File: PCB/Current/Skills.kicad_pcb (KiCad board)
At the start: 2 copper layers, 70 x 85 mm, 68 parts, among them J1 BATT, J2 USB_C_Receptacle_USB2.0, J3 SPI, J4 L, J5 R, U1 TPS61088, U2 FS312F, U3 FS8205A, U4 TP4056, U5 F-3188, U6 MAX9744, U7 ME6209

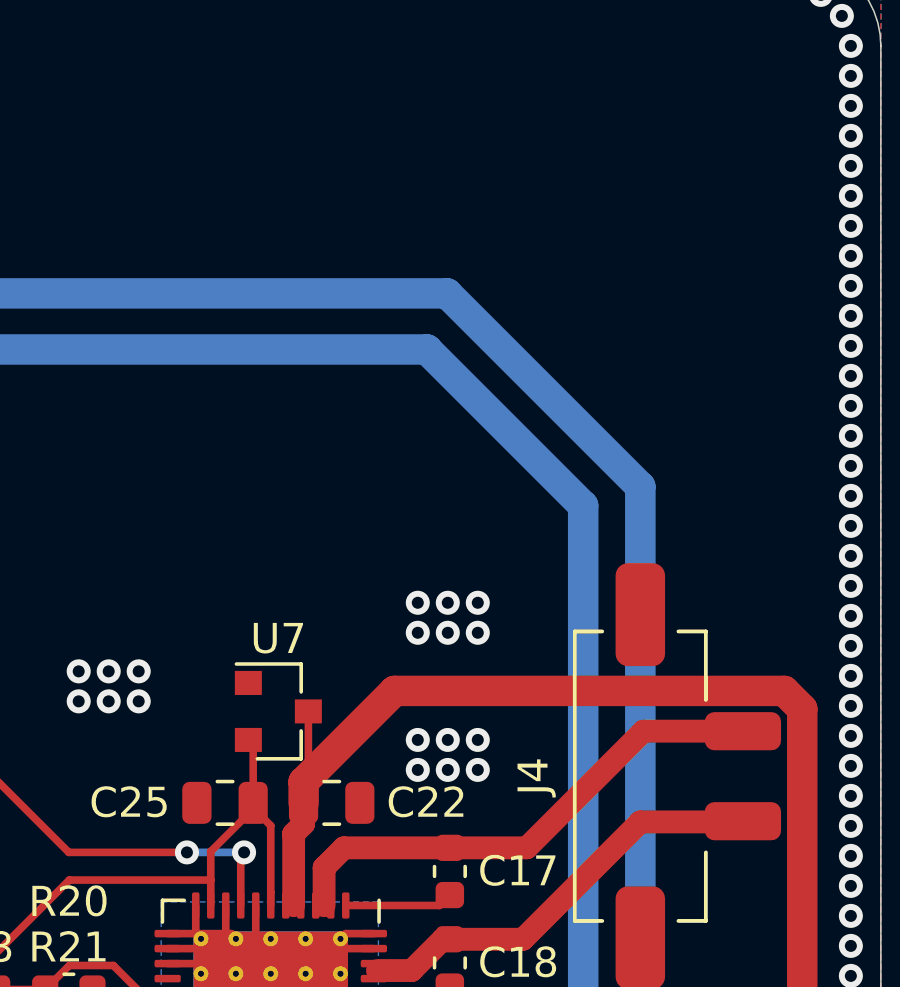
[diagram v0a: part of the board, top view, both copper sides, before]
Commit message: add KicCad logo
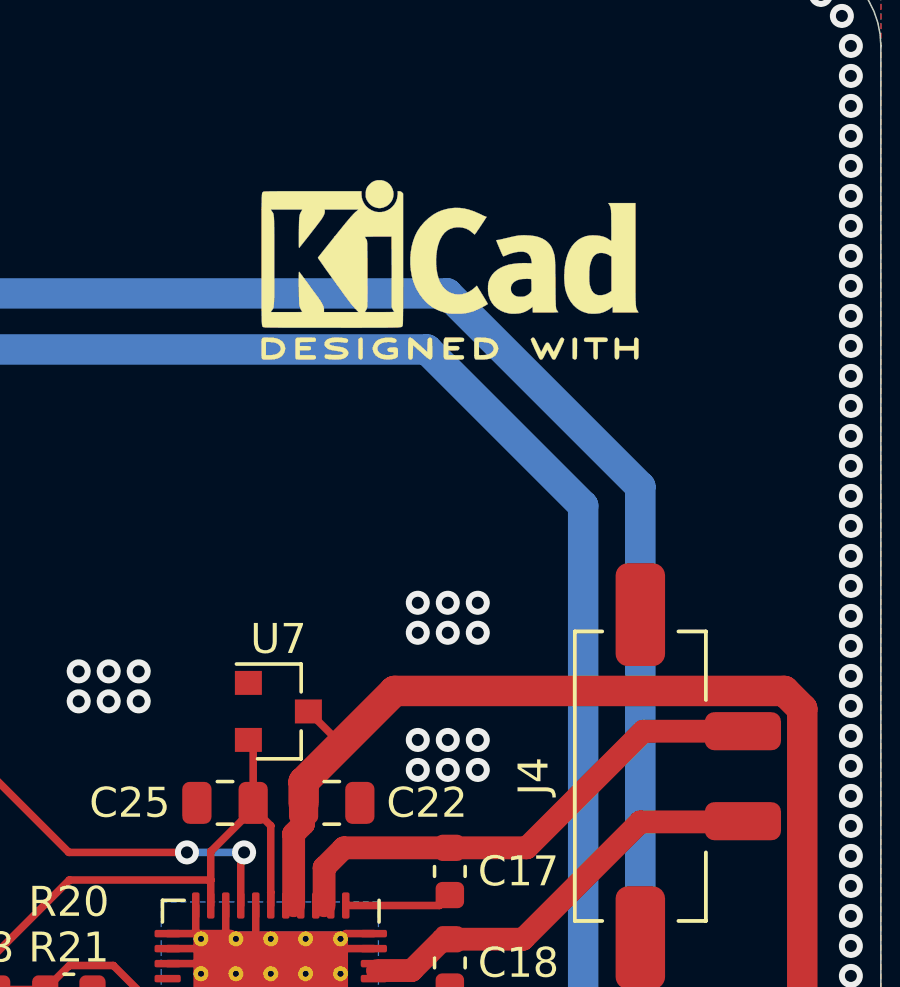
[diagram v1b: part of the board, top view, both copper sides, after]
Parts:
- added REF**: KiCad-Logo2_5mm_SilkScreen, Symbol:KiCad-Logo2_5mm_SilkScreen, F.Cu at (103.6, 60.5)

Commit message: working
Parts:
- removed REF**: KiCad-Logo2_5mm_SilkScreen, Symbol:KiCad-Logo2_5mm_SilkScreen
- C1, C11, C8, C9: footprint Capacitor_SMD:C_0805_2012Metric -> Capacitor_SMD:C_1206_3216Metric
- moved C9 1.61 mm to (74.5, 107.7)
- moved C16 1.59 mm to (69.5, 112.0)
- moved C8 1.14 mm to (77.2, 107.7)
- moved C11 0.52 mm to (93.3, 115.6)
- moved C1 0.19 mm to (96.0, 115.6)
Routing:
- net +12V: track 106.9 -> 107.6 mm
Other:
- board text added: "LSD-Speaker - Lorenz - Stefan - Damian"

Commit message: annotate
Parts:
- added REF**: KiCad-Logo2_5mm_SilkScreen, Symbol:KiCad-Logo2_5mm_SilkScreen, F.Cu at (102.5, 60.7)
- renumbered C4 to C1, C12 to C10, C2 to C11, C21 to C12, C22 to C13, C24 to C14, C25 to C15, C14 to C16, C15 to C18, C18 to C19, C11 to C2, C19 to C20, C20 to C21, C13 to C22, C1 to C3, C8 to C4, C9 to C5, C16 to C6, C3 to C7, C5 to C8, C6 to C9, D6 to D1, D1 to D2, D2 to D3, D3 to D4, D4 to D5, D5 to D6, J2 to J1, J1 to J2, J4 to J3, J3 to J4, R22 to R1, R9 to R10, R7 to R11, R14 to R13, R15 to R14, R18 to R15, R20 to R16, R16 to R17, R17 to R18, R4 to R2, R21 to R20, R11 to R21, R13 to R22, R1 to R3, R3 to R4, R2 to R6, R6 to R7, R10 to R8, R8 to R9, U4 to U2, U2 to U3, U3 to U4, U7 to U5, U5 to U6, U6 to U7

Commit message: emi
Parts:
- added C7: 100u, Capacitor_SMD:CP_Elec_6.3x7.7, F.Cu at (69.2, 100.3)
- added L2: L, Inductor_SMD:L_0805_2012Metric, F.Cu at (71.5, 109.1)
- C6: value 100u -> 22u; footprint Capacitor_SMD:CP_Elec_6.3x7.7 -> Capacitor_SMD:C_1206_3216Metric
- moved C6 5.63 mm to (70.7, 106.5), turned to 0 degrees
- renumbered C9 to C10, C10 to C11, C11 to C12, C12 to C13, C13 to C14, C14 to C15, C15 to C16, C16 to C17, C17 to C18, C18 to C19, C19 to C20, C20 to C21, C21 to C22, C22 to C23, C23 to C24, C7 to C8, C8 to C9
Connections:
- C4 pad 1: +12V -> Net-(C4-Pad1)
- C5 pad 1: +12V -> Net-(C4-Pad1)
- R2 pad 1: +12V -> Net-(C4-Pad1)
- U1 pad 14: +12V -> Net-(C4-Pad1)
- U1 pad 15: +12V -> Net-(C4-Pad1)
- U1 pad 16: +12V -> Net-(C4-Pad1)
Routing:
- net +12V: track 107.6 -> 109.0 mm
- net GND: vias 335 -> 347
- added copper zone on F.Cu, net Net-(C4-Pad1)
- removed copper zone on F.Cu, net +12V
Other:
- board text added: "+"
- board text added: "-"
- board text added: "Damian Stefan Lorenz"
- board text removed: "LSD-Speaker - Lorenz - Stefan - Damian"
